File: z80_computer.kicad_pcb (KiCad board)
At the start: 2 copper layers, 15 parts, among them J7 CompactFlash Port, U12 Z84C40-SIO-0, U24 OPEN-SMART-3.5

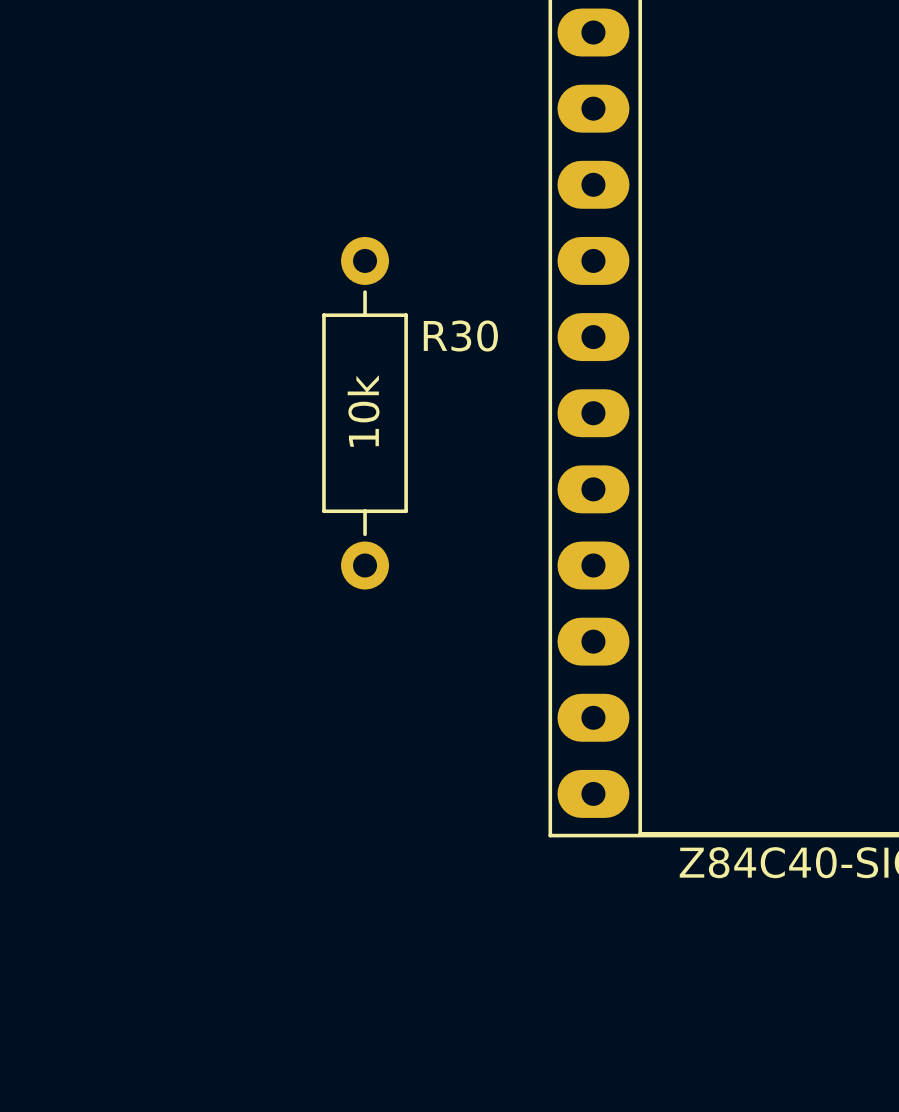
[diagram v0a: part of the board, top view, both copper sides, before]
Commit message: Revision 2 bug fix. NMI / INT reversed. Added resistors to UART Rx/Tx
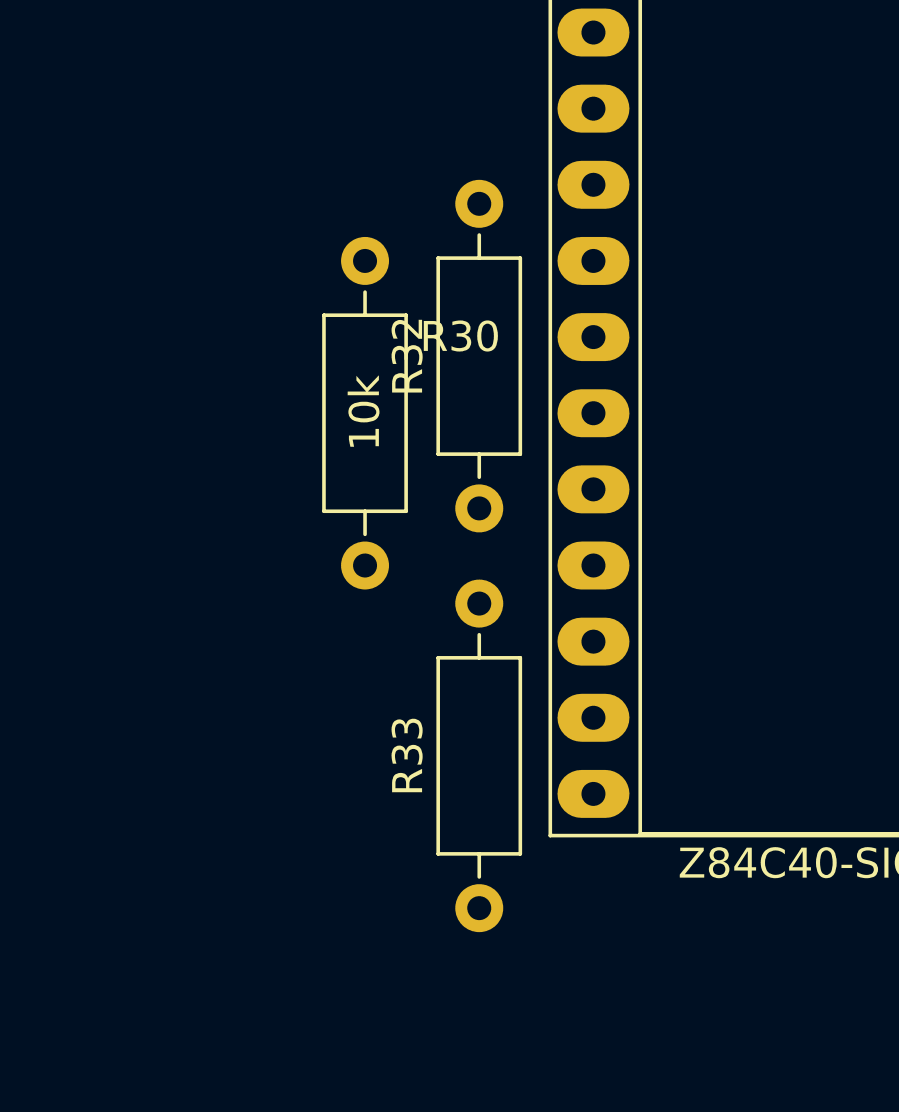
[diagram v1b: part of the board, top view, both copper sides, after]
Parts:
- added R32: 2k7, Resistor_THT:R_Axial_DIN0207_L6.3mm_D2.5mm_P10.16mm_Horizontal, F.Cu at (259.1, 155.6)
- added R33: 2k7, Resistor_THT:R_Axial_DIN0207_L6.3mm_D2.5mm_P10.16mm_Horizontal, F.Cu at (259.1, 168.9)
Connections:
- U12 pad 12: /Input Output/RXD -> Net-(R32-Pad2)
- U12 pad 15: /Input Output/TXD -> Net-(R33-Pad2)
